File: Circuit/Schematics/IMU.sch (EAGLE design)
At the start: 19 parts, among them IC1 REG1117F

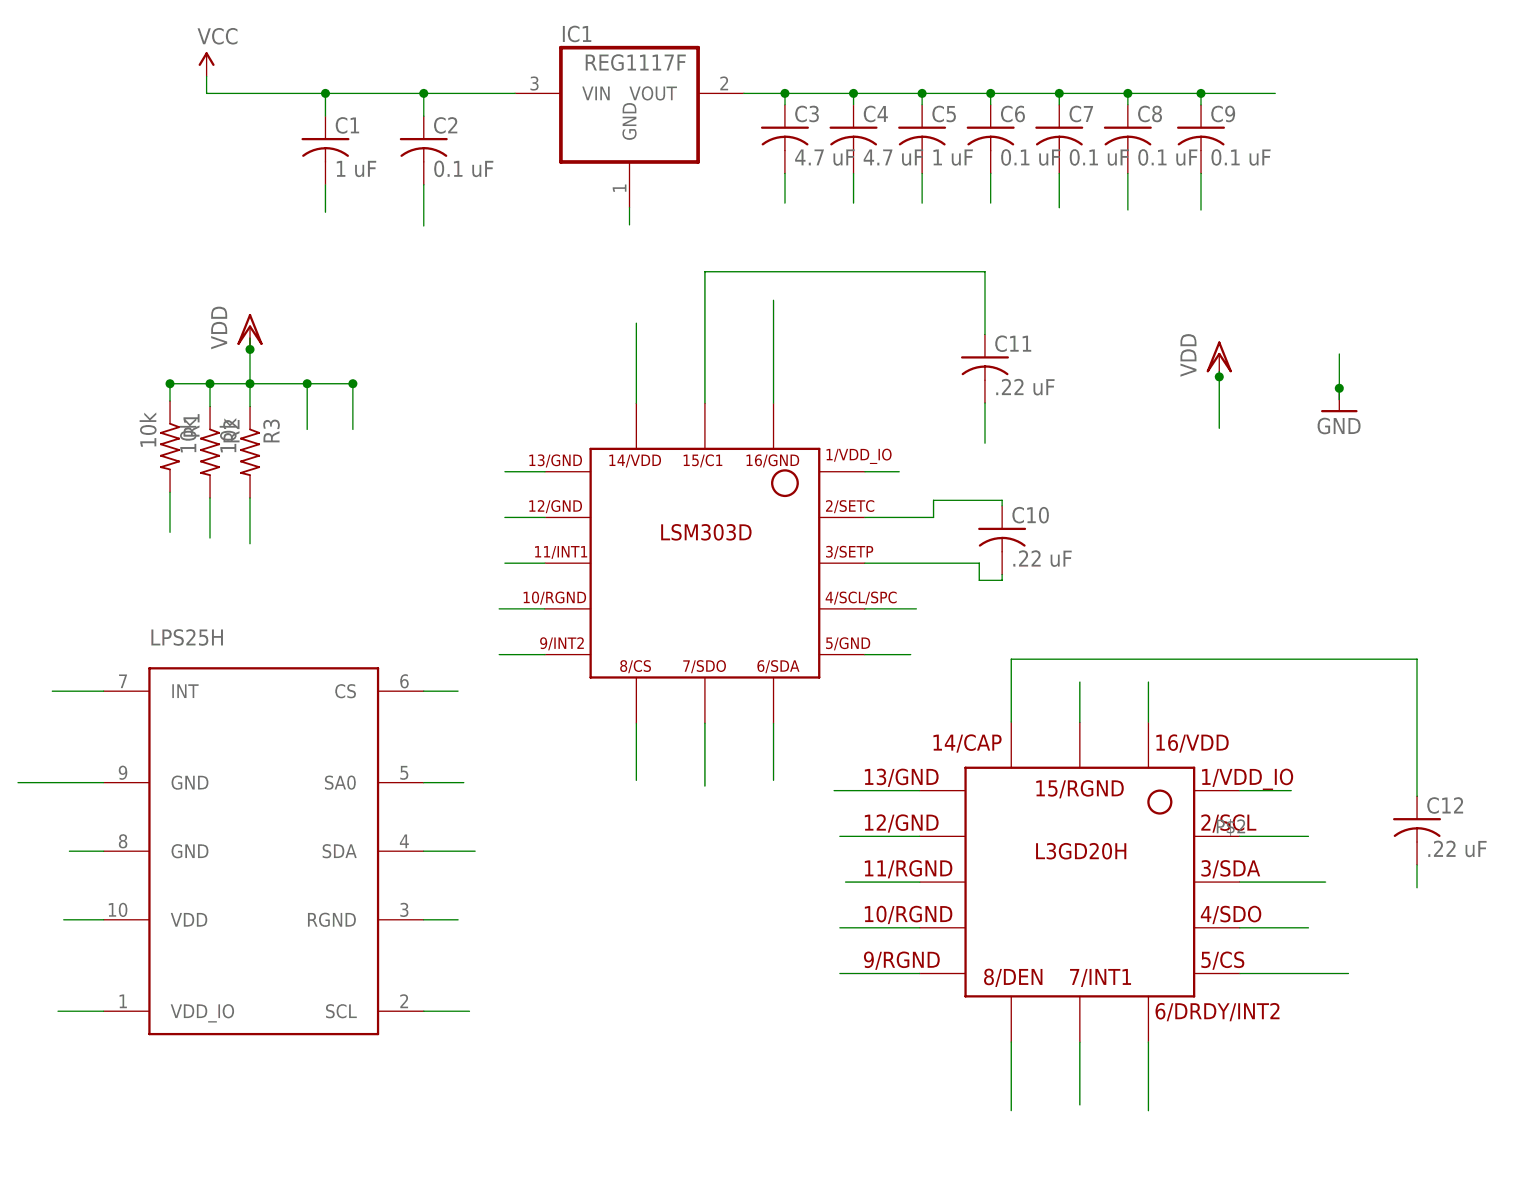
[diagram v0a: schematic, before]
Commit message: IMU, Wifi, Mesh schematics up, need reivision. Teensy untouched and must be designed
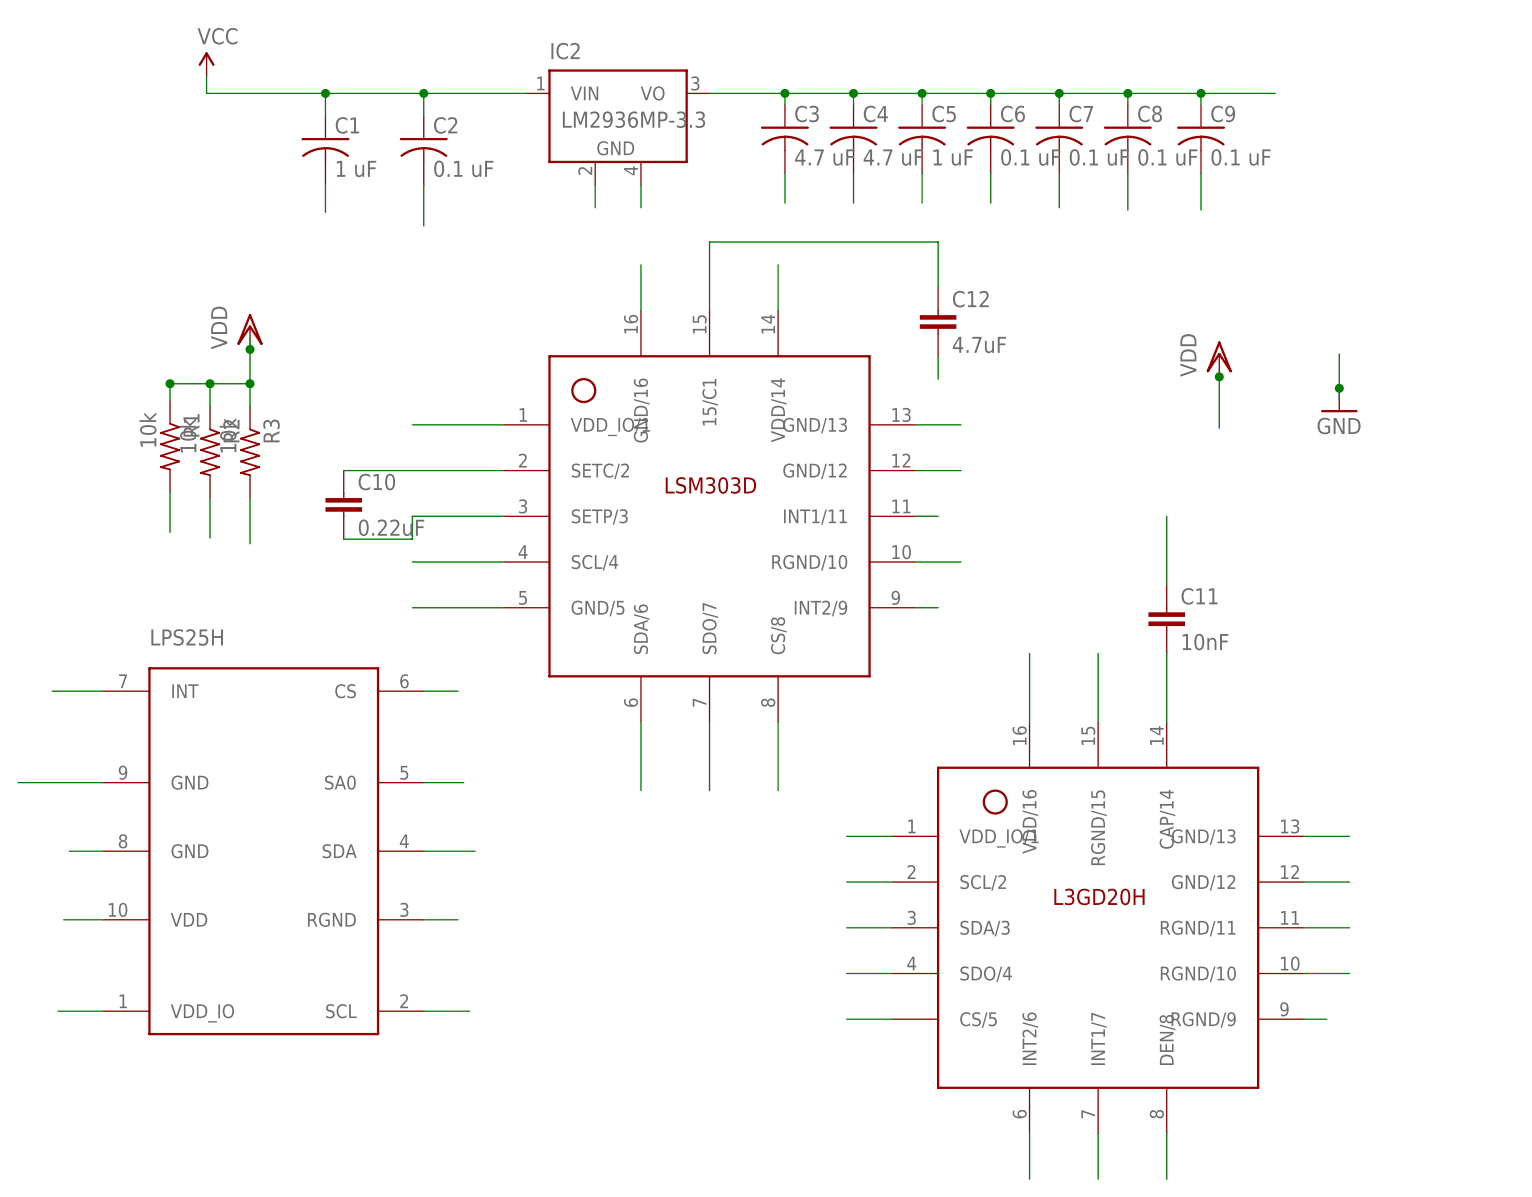
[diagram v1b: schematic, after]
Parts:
- removed IC1: REG1117F, burr-brown:REG1117F
- added IC2: LM2936MP-3.3, national-semiconductor:LM2936MP-3.3
- C10: value .22 uF -> 0.22uF; device adafruit:C-USC0805 -> SparkFun-Capacitors:0.22UF50V-20%,+80%(0603)
- C11: value .22 uF -> 10nF; device adafruit:C-USC0805 -> SparkFun-Capacitors:10NF/10000PF-50V-10%(0603)
- C12: value .22 uF -> 4.7uF; device adafruit:C-USC0805 -> SparkFun-Capacitors:4.7UF-6.3V-10%(0603)0603
- U$1: value LSM303D -> L3GD20H; device IMU_chips:LSM303D -> IMU_chips:L3GD20H
- U$2: value L3GD20H -> LSM303D; device IMU_chips:L3GD20H -> IMU_chips:LSM303D
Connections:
- removed net N$12: U$1.9/INT2
- removed net N$14: U$1.11/INT1
- removed net N$29: C12.1, U$2.14/CAP
- removed net N$35: U$2.6/DRDY/INT2
- removed net N$36: U$2.7/INT1
- removed net N$37: U$2.8/DEN
- removed net N$4: C11.1, U$1.15/C1
- removed net N$5: C10.2, U$1.3/SETP
- removed net N$8: U$1.5/GND
- new net N$11: U$2.INT1/11
- new net N$15: C12.1, U$2.15/C1
- new net N$2: C10.1, U$2.SETC/2
- new net N$24: U$1.INT2/6
- new net N$25: U$1.INT1/7
- new net N$32: C11.2, U$1.CAP/14
- new net N$9: U$2.INT2/9
- net GND: now also C11.1, IC2.GND@1, IC2.GND@2, U$1.DEN/8, U$1.GND/12, U$1.GND/13, U$1.RGND/10, U$1.RGND/11, U$1.RGND/9, U$1.VDD/16, U$2.GND/12, U$2.GND/13, U$2.GND/16, U$2.GND/5, U$2.RGND/10; no longer C11.2, IC1.GND, U$1.10/RGND, U$1.12/GND, U$1.13/GND, U$1.16/GND, U$2.10/RGND, U$2.11/RGND, U$2.12/GND, U$2.13/GND, U$2.15/RGND, U$2.9/RGND
- net N$3: now also C10.2, U$2.SETP/3; no longer C10.1, U$1.2/SETC
- net SCL: now also U$1.SCL/2, U$2.SCL/4; no longer U$1.4/SCL/SPC, U$2.2/SCL
- net SDA: now also U$1.SDA/3, U$2.SDA/6; no longer U$1.6/SDA/SDI/SDO, U$2.3/SDA
- net SDO: now also U$1.SDO/4, U$2.SDO/7; no longer U$1.7/SDO/SA0, U$2.4/SDO
- net VCC: now also IC2.VIN; no longer IC1.VIN
- net VDD: now also IC2.VO, U$1.CS/5, U$1.RGND/15, U$1.VDD_IO/1, U$2.CS/8, U$2.VDD/14, U$2.VDD_IO/1; no longer IC1.VOUT, U$1.1/VDD_IO, U$1.14/VDD, U$1.8/CS, U$2.1/VDD_IO, U$2.16/VDD, U$2.5/CS
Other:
- moved on the sheet: C10, C11, C12
